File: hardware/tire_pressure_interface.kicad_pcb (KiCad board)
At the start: 4 copper layers, 80.2 x 65.5 mm, 81 parts, among them IC1 TPS54202HDDCR, J3 FTSH-107-01-L-D-K, J4 Conn_02x02_Counter_Clockwise, J5 Micro_SD_Card_Det1, Q1 SI2347DS-T1-GE3, T1 TP_+3V3, T10 TP_+5V, T11 TP_+5V, T3 TP_VCC, T8 TP_VCC, T9 TP_+3V3, U1 STM32G0C1KCTxN, U2 LM1117-3.3, U3 XIAO-ESP32-S3-DIP, U7 ADM3057ExRW

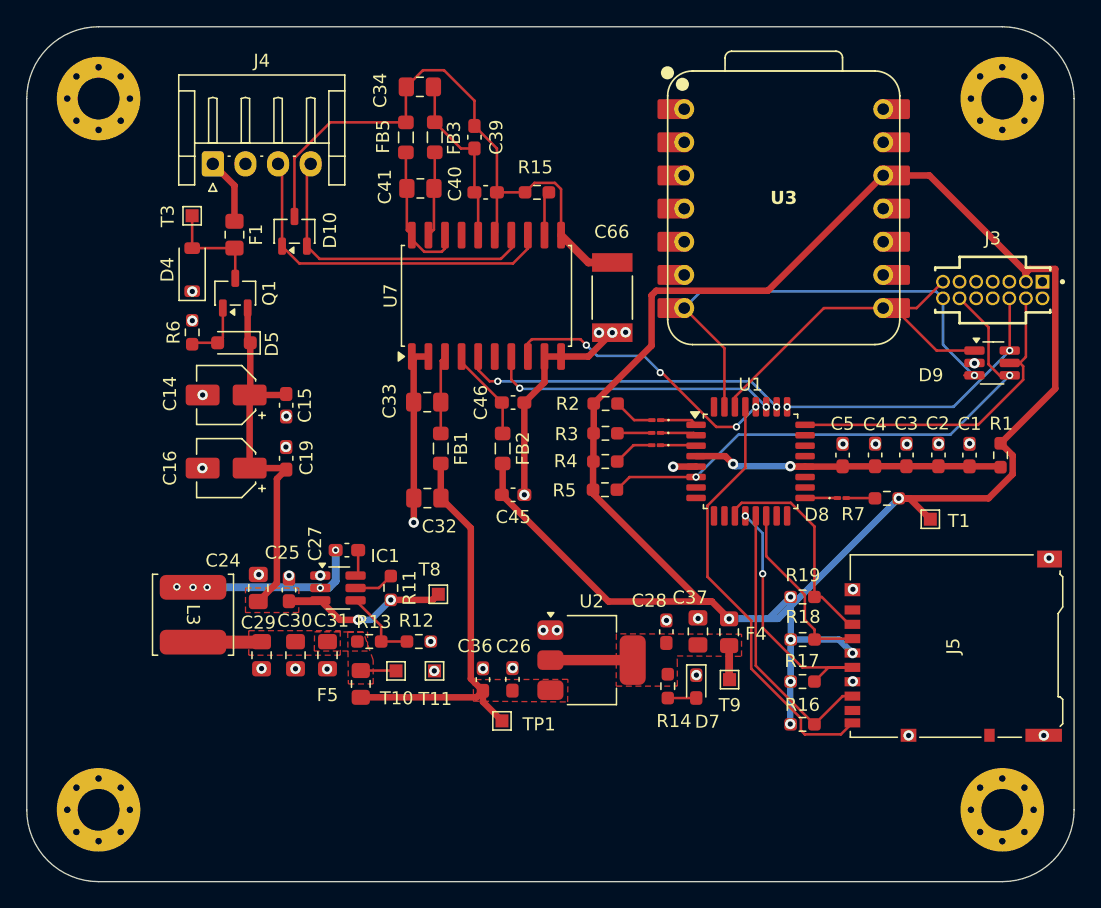
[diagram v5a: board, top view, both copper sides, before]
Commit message: changed layout
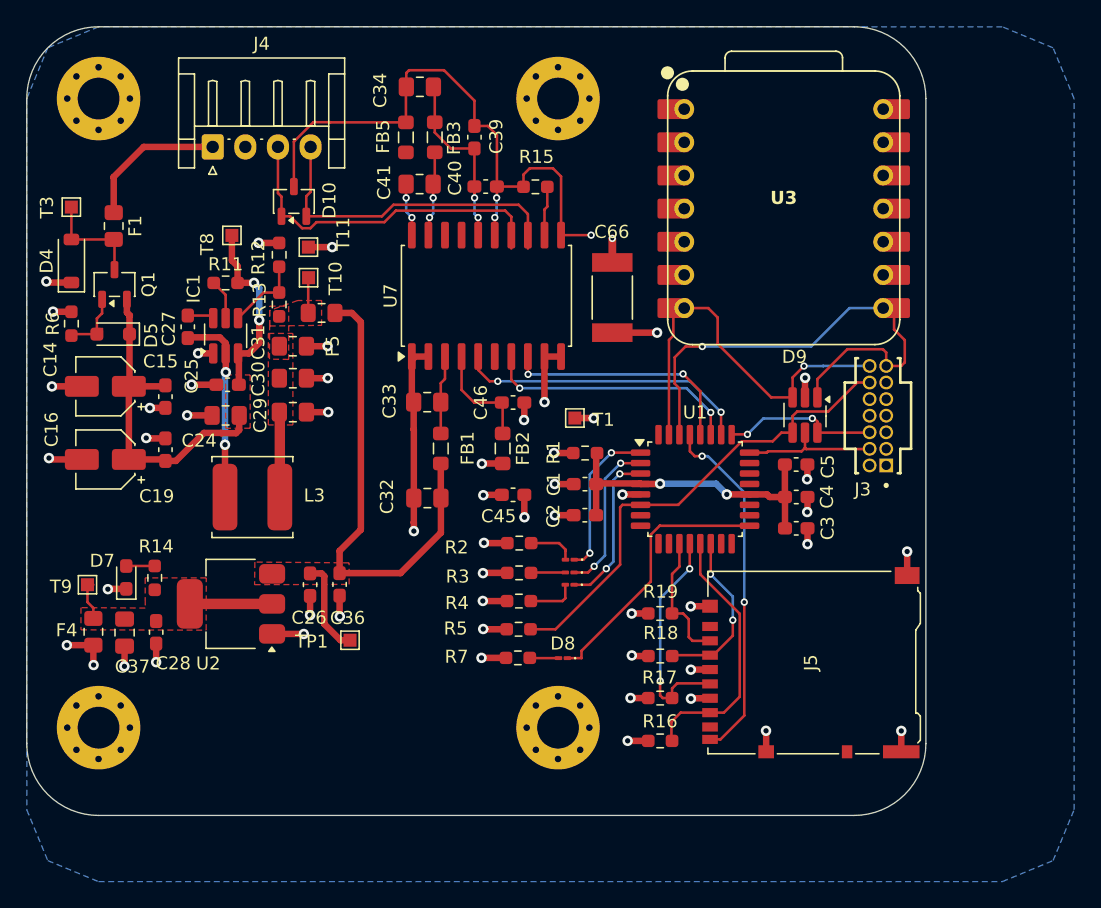
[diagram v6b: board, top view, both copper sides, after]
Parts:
- moved REF** 64.2 mm to (110.5, 79.3)
- moved REF** 59.0 mm to (110.5, 127.5)
- moved T9 49.7 mm to (74.5, 116.6), turned to 180 degrees
- moved F4 48.7 mm to (74.9, 120.2), turned to 90 degrees
- moved D7 44.5 mm to (77.4, 116.0), turned to 90 degrees
- moved C37 43.9 mm to (77.3, 120.2), turned to -90 degrees
- moved R14 40.2 mm to (79.6, 116.0), turned to 90 degrees
- moved C28 39.1 mm to (79.7, 120.2), turned to -90 degrees
- moved T11 33.9 mm to (91.4, 90.7), turned to 90 degrees
- moved R1 31.8 mm to (112.6, 106.5), turned to 0 degrees
- moved T8 31.7 mm to (85.5, 89.8), turned to 90 degrees
- moved R12 31.5 mm to (89.1, 91.3), turned to -90 degrees
- moved T10 30.9 mm to (91.4, 93.0), turned to 90 degrees
- moved R7 30.8 mm to (107.4, 122.2), turned to 180 degrees
- moved C1 29.5 mm to (112.6, 108.9), turned to 180 degrees
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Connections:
- D10 pad 1: /Connectors/CAN.L -> /Connectors/CAN_N
- D10 pad 2: /Connectors/CAN.H -> /Connectors/CAN_P
- J4 pad 3: /Connectors/CAN.L -> /Connectors/CAN_N
- J4 pad 4: /Connectors/CAN.H -> /Connectors/CAN_P
- U7 pad 13: /Connectors/CAN.L -> /Connectors/CAN_P
- U7 pad 14: /Connectors/CAN.H -> /Connectors/CAN_N
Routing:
- net +3V3: track 160.3 -> 25.9 mm, vias 7 -> 16
- net GND: track 40.8 -> 83.7 mm, vias 38 -> 37
- net /Connectors/CAN.L: track 27.3 -> 0.00 mm
- net /Connectors/CAN_N: track 0.00 -> 26.6 mm
- net /Connectors/CAN_P: track 0.00 -> 25.7 mm
- net /Connectors/CAN.H: track 23.8 -> 0.00 mm
- net /STM32/LED.ACT: track 2.48 -> 20.6 mm
- net /Connectors/SWDIO: track 25.4 -> 10.6 mm
- net +5V: track 31.2 -> 43.9 mm
- net /RX: track 27.5 -> 38.9 mm, vias 0 -> 1
- net /Connectors/SWCLK: track 22.9 -> 12.0 mm
- net /STM32/LED.ERR: track 2.74 -> 12.3 mm, vias 0 -> 2
- net /STM32/LED.OK: track 2.86 -> 12.0 mm, vias 0 -> 2
- net /STM32/LED.WRN: track 3.55 -> 12.0 mm, vias 0 -> 2
- net /TX: track 37.1 -> 29.9 mm
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- added copper zone on B.Cu, net +3V3
- added copper zone on In1.Cu, net /CAN_BUS/GND_CAN_ISO1
- added copper zone on In2.Cu, net /CAN_BUS/GND_CAN_ISO1
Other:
- board size 80.2 x 65.5 mm -> 68.9 x 60.4 mm

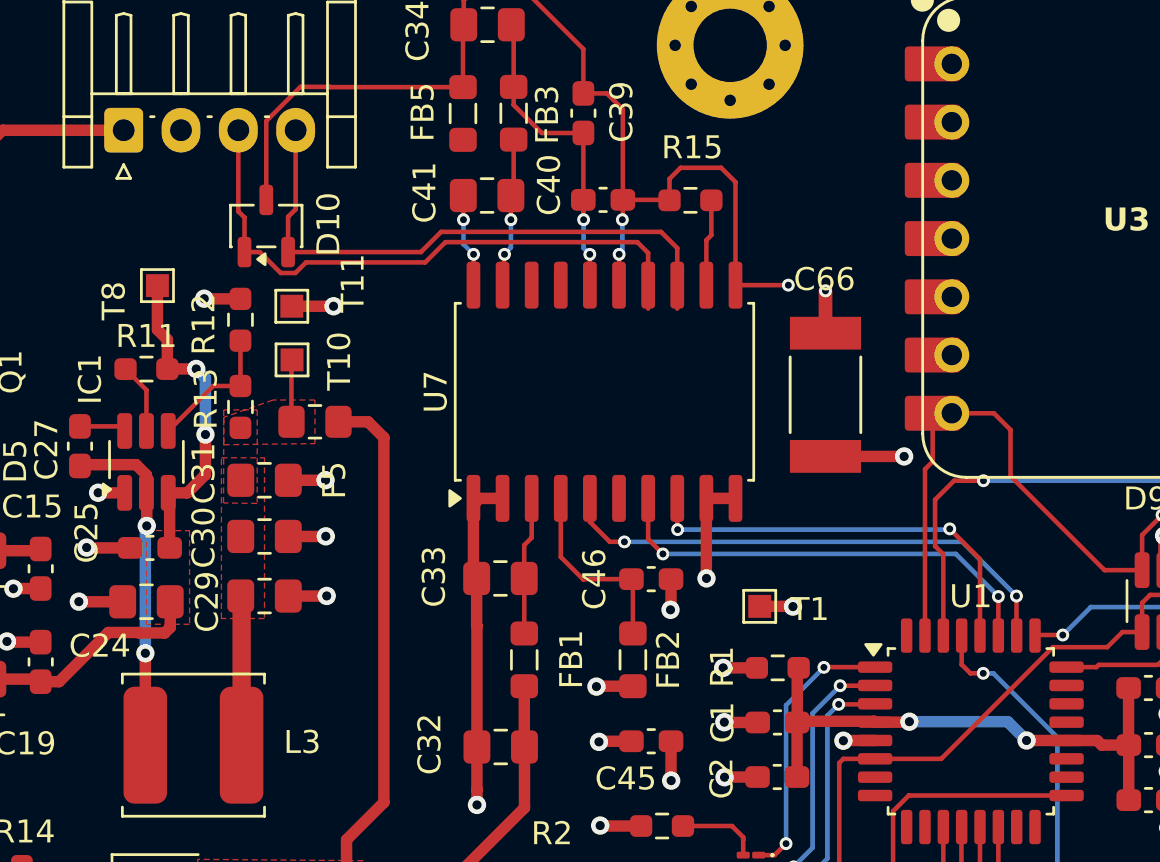
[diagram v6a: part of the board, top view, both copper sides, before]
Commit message: fixed drc issues
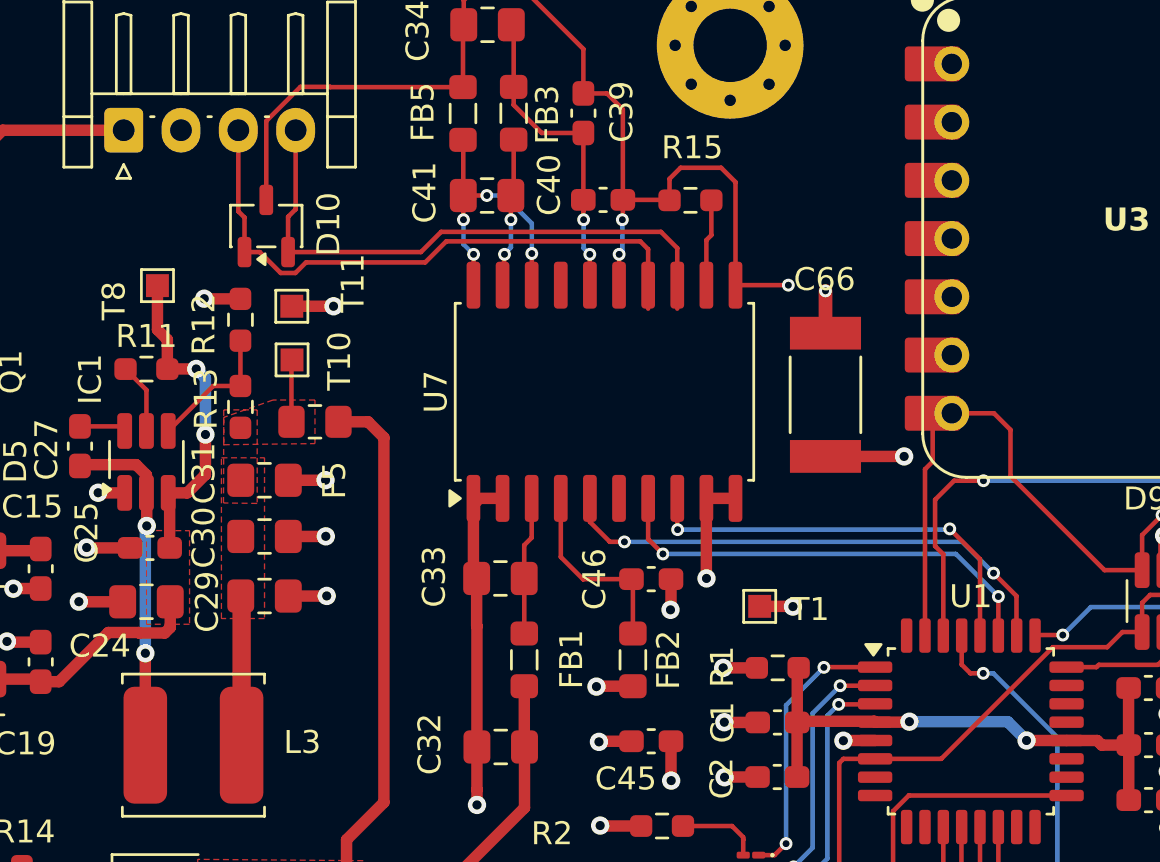
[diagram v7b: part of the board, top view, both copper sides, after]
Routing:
- net Net-(C41-Pad1): track 4.62 -> 13.2 mm, vias 2 -> 4

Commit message: changed pcb layout
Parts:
- D1, D2, D3, D8: footprint LED_SMD:LED_01005_0402Metric_Pad0.57x0.30mm_HandSolder -> LED_SMD:LED_0603_1608Metric_Pad1.05x0.95mm_HandSolder
- moved U3 51.3 mm to (91.0, 123.5), turned to 180 degrees
- moved REF** 40.7 mm to (125.6, 89.7)
- moved REF** 39.7 mm to (125.6, 116.1)
- moved F4 32.4 mm to (89.5, 91.3), turned to 0 degrees
- moved T9 31.8 mm to (93.1, 90.8), turned to 90 degrees
- moved C32 31.3 mm to (95.3, 79.1), turned to -90 degrees
- moved C37 29.2 mm to (89.5, 93.7), turned to 180 degrees
- moved C45 27.8 mm to (96.4, 84.0), turned to -90 degrees
- moved T11 27.6 mm to (72.8, 111.1), turned to -90 degrees
- moved D7 27.5 mm to (93.7, 93.8), turned to 0 degrees
- moved C34 26.9 mm to (126.8, 78.5), turned to -90 degrees
- moved R5 26.1 mm to (125.9, 101.4), turned to -90 degrees
- moved FB1 26.1 mm to (99.1, 80.1), turned to 180 degrees
- moved C28 26.0 mm to (89.5, 96.1), turned to 180 degrees
- moved FB5 24.5 mm to (122.9, 77.5), turned to 180 degrees
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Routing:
- net /Connectors/CAN_P: track 25.7 -> 75.9 mm
- net /Connectors/CAN_N: track 26.7 -> 74.5 mm
- net /TX: track 29.9 -> 64.8 mm, vias 1 -> 2
- net /STM32/LED.ERR: track 12.3 -> 42.6 mm
- net /STM32/LED.OK: track 12.0 -> 40.4 mm
- net /STM32/LED.WRN: track 12.0 -> 39.0 mm
- net /STM32/STM_VCC: track 24.7 -> 47.3 mm
- net /Power/VCC_IN: track 40.4 -> 19.0 mm, vias 2 -> 0
- net /CAN_BUS/GND_CAN_ISO1: track 49.6 -> 67.5 mm
- net /RX: track 38.9 -> 49.9 mm
- net /Micro_SD_Card/SCK: track 17.4 -> 7.77 mm
- net /Connectors/SWDIO: track 10.6 -> 20.0 mm
- net /Micro_SD_Card/DET: track 27.2 -> 18.2 mm, vias 2 -> 0
- net GND: track 83.7 -> 74.8 mm, vias 37 -> 38
- net /Micro_SD_Card/MISO: track 20.5 -> 13.0 mm
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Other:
- board size 68.9 x 60.4 mm -> 60.3 x 60.4 mm
- board text added: "D4"
